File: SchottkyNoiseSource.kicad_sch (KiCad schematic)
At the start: 42 parts, among them J1 Conn_Coaxial, J2 Conn_01x02, J3 Conn_01x02, J4 Conn_Coaxial, J5 Conn_01x02, J6 Conn_Coaxial

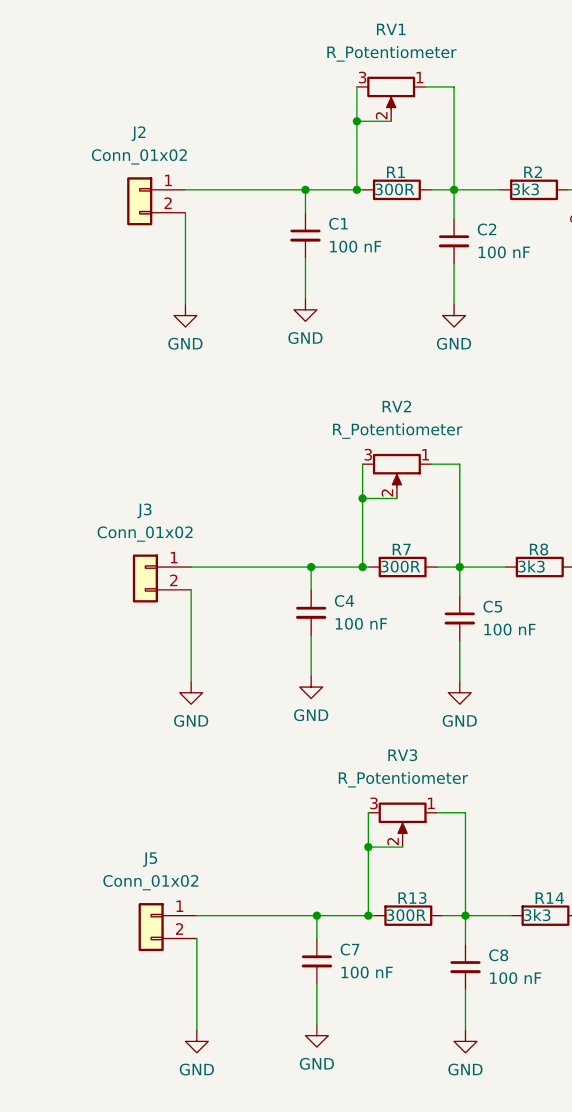
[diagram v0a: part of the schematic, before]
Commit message: Rearranged components slightly, removed solder mask to allow shield to be fitted
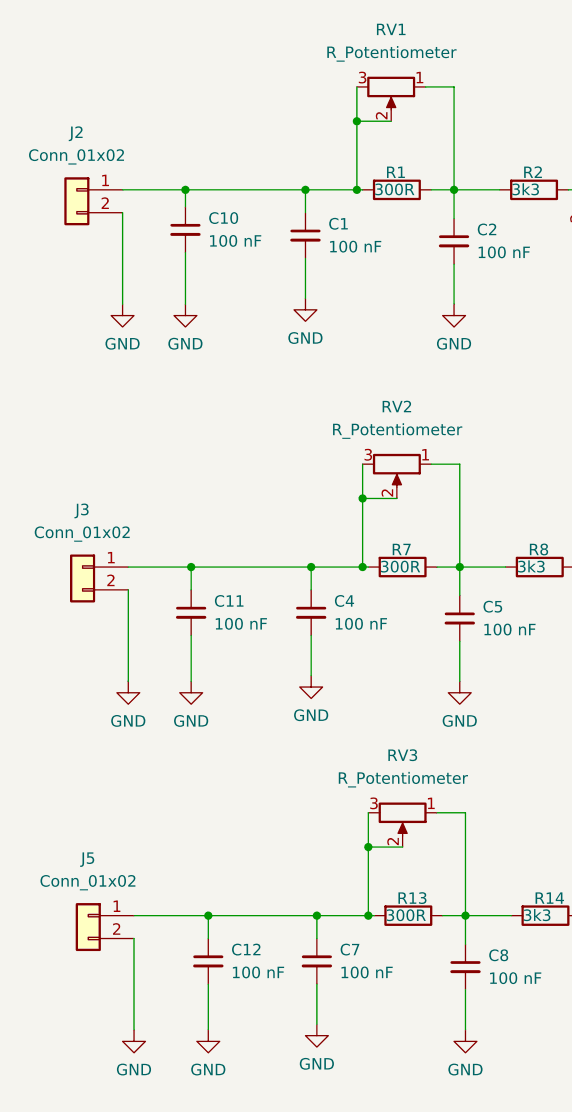
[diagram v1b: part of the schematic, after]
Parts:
- added C10, C11, C12: 100 nF, Capacitor_SMD:C_0402_1005Metric_Pad0.74x0.62mm_HandSolder, symbol Device:C_Small
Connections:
- net GND: now also C10.2, C11.2, C12.2
- net at C7.1, J5.1 (Pin_1), R13.2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: now also C12.1
- net at C4.1, J3.1 (Pin_1), R7.2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: now also C11.1
- net at C1.1, J2.1 (Pin_1), R1.2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: now also C10.1
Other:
- moved on the sheet: J2, J3, J5

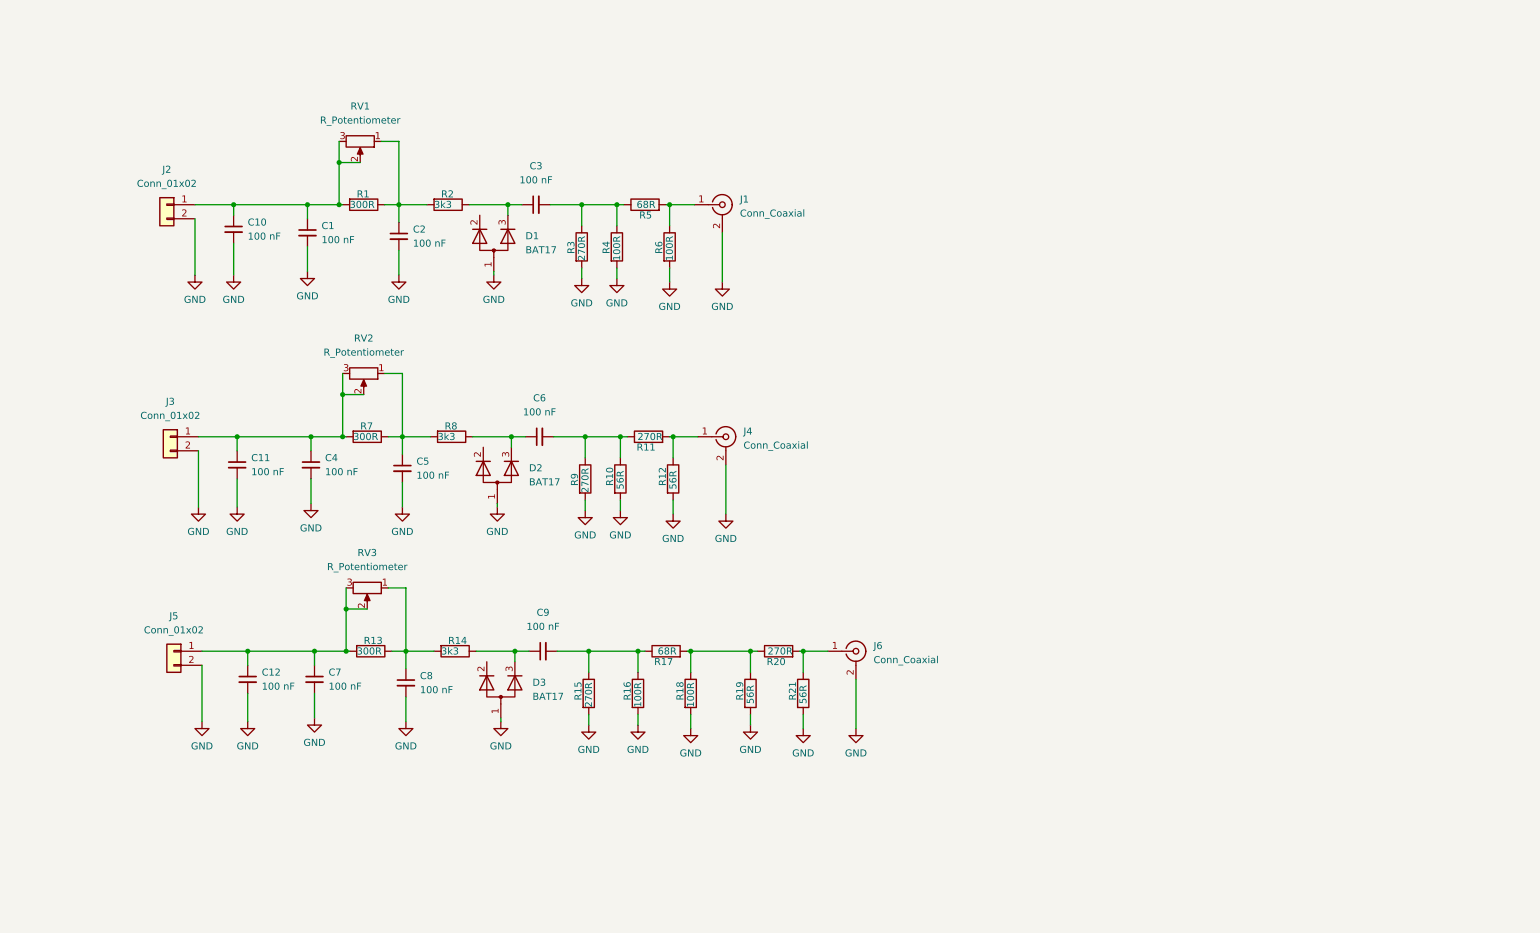
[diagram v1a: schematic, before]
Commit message: Added sense diode to noise sources
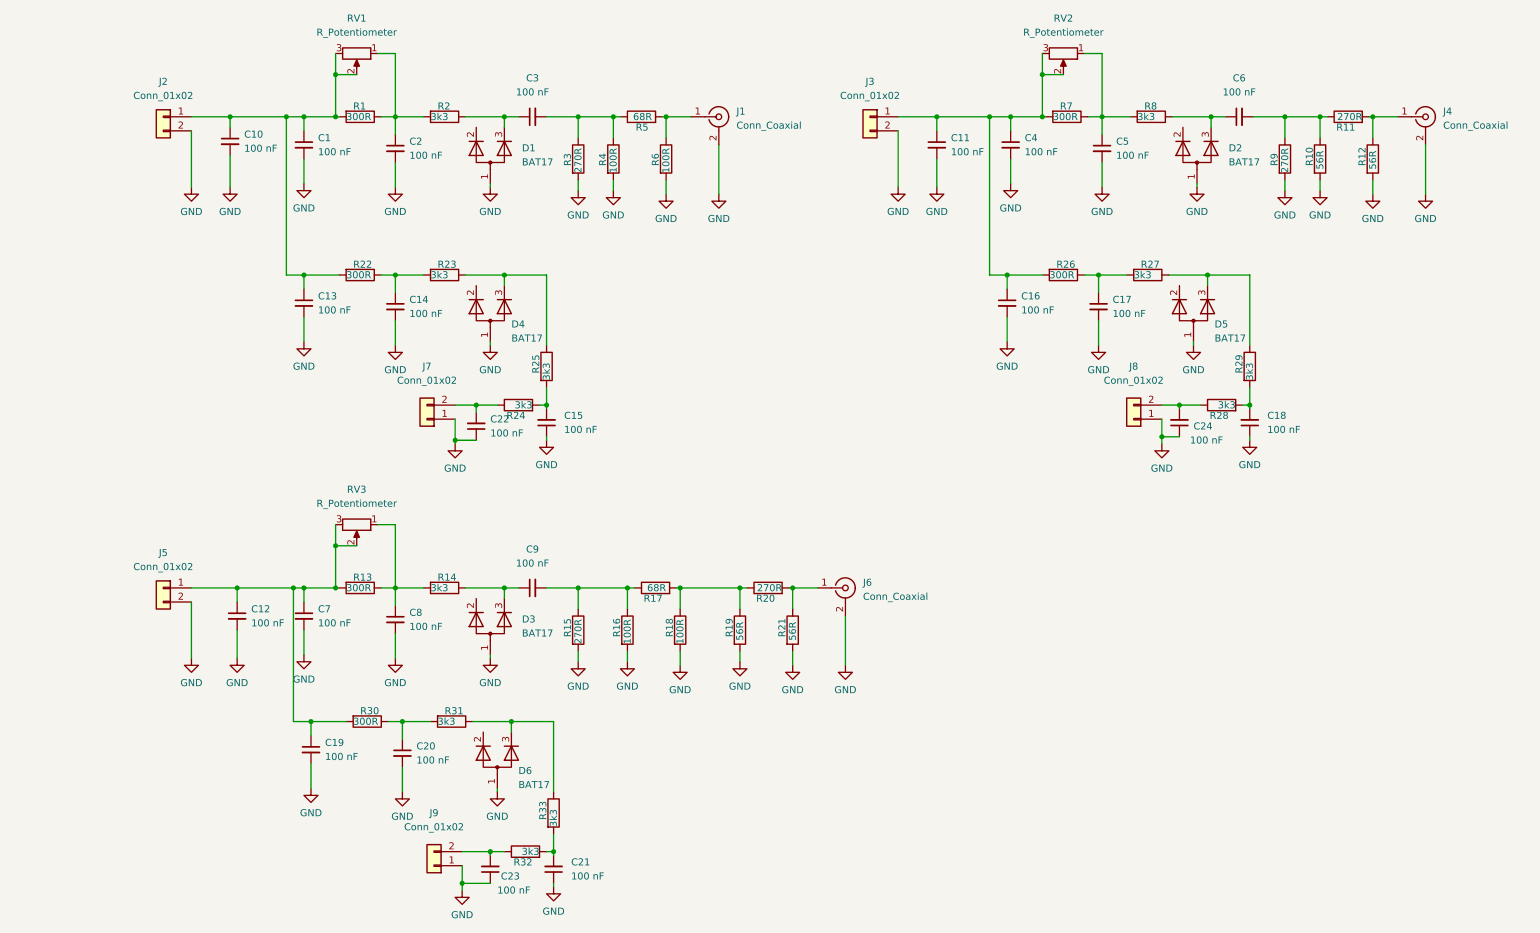
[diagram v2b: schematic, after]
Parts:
- added C13, C14, C15, C16, C17, C18, C19, C20, C21, C22, C23, C24: 100 nF, Capacitor_SMD:C_0402_1005Metric_Pad0.74x0.62mm_HandSolder, symbol Device:C_Small
- added D4, D5, D6: BAT17, Package_TO_SOT_SMD:SOT-23, symbol Device:D_Dual_CommonAnode_AKK_Parallel
- added J7, J8, J9: Conn_01x02, Connector_PinHeader_2.54mm:PinHeader_1x02_P2.54mm_Vertical, symbol Connector_Generic:Conn_01x02
- added R22, R26, R30: 300R, Resistor_SMD:R_0805_2012Metric_Pad1.20x1.40mm_HandSolder, symbol Device:R
- added R23, R24, R25, R27, R28, R29, R31, R32, R33: 3k3, Resistor_SMD:R_0603_1608Metric_Pad0.98x0.95mm_HandSolder, symbol Device:R
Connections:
- net GND: now also C13.2, C14.2, C15.1, C16.2, C17.2, C18.1, C19.2, C20.2, C21.1, C22.1, C23.1, C24.1, D4.1 (A), D5.1 (A), D6.1 (A), J7.1 (Pin_1), J8.1 (Pin_1), J9.1 (Pin_1)
- net at C12.1, C7.1, J5.1 (Pin_1)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: now also C19.1, R30.2
- net at C11.1, C4.1, J3.1 (Pin_1)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: now also C16.1, R26.2
- net at C1.1, C10.1, J2.1 (Pin_1)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: now also C13.1, R22.2
- new net: C23.2, J9.2 (Pin_2), R32.1
- new net: C14.1, R22.1, R23.2
- new net: D5.3 (K), R27.1, R29.1
- new net: D4.3 (K), R23.1, R25.1
- new net: C15.2, R24.2, R25.2
- new net: C24.2, J8.2 (Pin_2), R28.1
- new net: D6.3 (K), R31.1, R33.1
- new net: C21.2, R32.2, R33.2
- new net: C17.1, R26.1, R27.2
- new net: C22.2, J7.2 (Pin_2), R24.1
- new net: C18.2, R28.2, R29.2
- new net: C20.1, R30.1, R31.2
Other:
- moved on the sheet: C1, C10, C11, C12, C2, C3, C4, C5, C6, C7, C8, C9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

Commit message: Added heater resistors
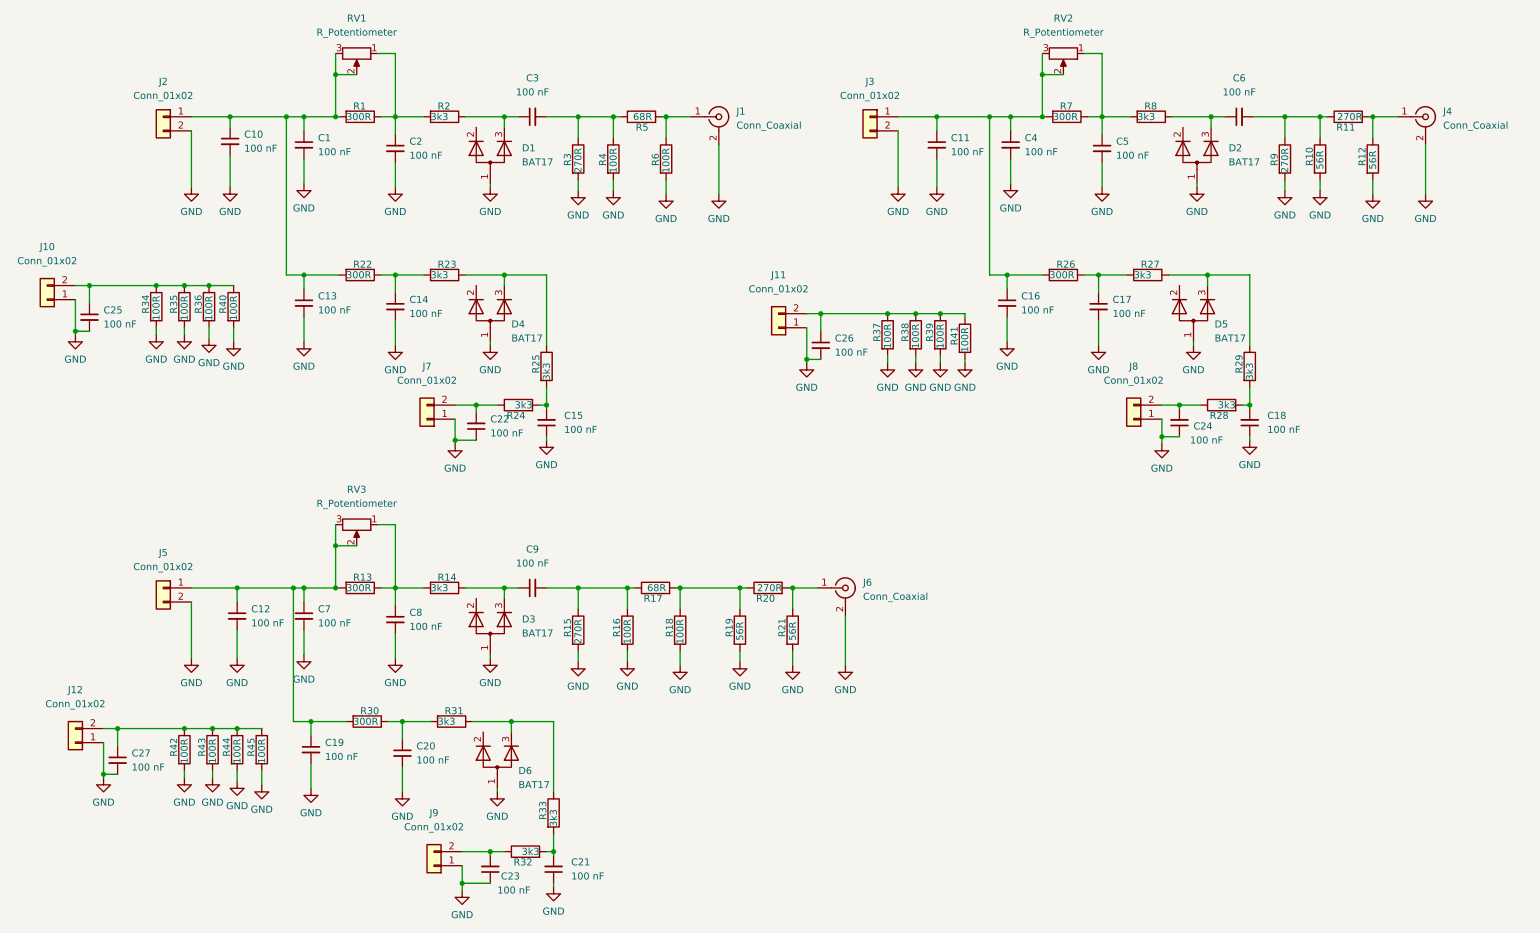
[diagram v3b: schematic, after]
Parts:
- added C25, C26, C27: 100 nF, Capacitor_SMD:C_0402_1005Metric_Pad0.74x0.62mm_HandSolder, symbol Device:C_Small
- added J10, J11, J12: Conn_01x02, Connector_PinHeader_2.54mm:PinHeader_1x02_P2.54mm_Vertical, symbol Connector_Generic:Conn_01x02
- added R34, R35, R36, R37, R38, R39, R40, R41, R42, R43, R44, R45: 100R, Resistor_SMD:R_1206_3216Metric_Pad1.30x1.75mm_HandSolder, symbol Device:R
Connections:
- net GND: now also C25.2, C26.2, C27.2, J10.1 (Pin_1), J11.1 (Pin_1), J12.1 (Pin_1), R34.2, R35.2, R36.2, R37.2, R38.2, R39.2, R40.2, R41.2, R42.2, R43.2, R44.2, R45.2
- new net: C27.1, J12.2 (Pin_2), R42.1, R43.1, R44.1, R45.1
- new net: C25.1, J10.2 (Pin_2), R34.1, R35.1, R36.1, R40.1
- new net: C26.1, J11.2 (Pin_2), R37.1, R38.1, R39.1, R41.1

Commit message: Made pin header connector
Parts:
- J2, J3, J5: footprint TerminalBlock:TerminalBlock_bornier-2_P5.08mm -> Connector_PinHeader_2.54mm:PinHeader_1x02_P2.54mm_Vertical
- R34, R35, R36, R37, R38, R39, R40, R41, R42, R43, R44, R45: value 100R -> 4k7; LCSC C17901 -> C17936
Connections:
- net GND: now also J2.1 (Pin_1), J3.1 (Pin_1), J5.1 (Pin_1); no longer J2.2 (Pin_2), J3.2 (Pin_2), J5.2 (Pin_2)
- net at C1.1, C10.1, C13.1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: now also J2.2 (Pin_2); no longer J2.1 (Pin_1)
- net at C12.1, C19.1, C7.1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: now also J5.2 (Pin_2); no longer J5.1 (Pin_1)
- net at C11.1, C16.1, C4.1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: now also J3.2 (Pin_2); no longer J3.1 (Pin_1)
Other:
- moved on the sheet: J2, J3, J5
